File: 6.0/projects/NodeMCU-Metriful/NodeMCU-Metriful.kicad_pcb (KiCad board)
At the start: 2 copper layers, 5 parts, among them J3 DS18b20, J4 Particle, U1 NodeMCU_1.0_(ESP-12E), U2 Metriful-1

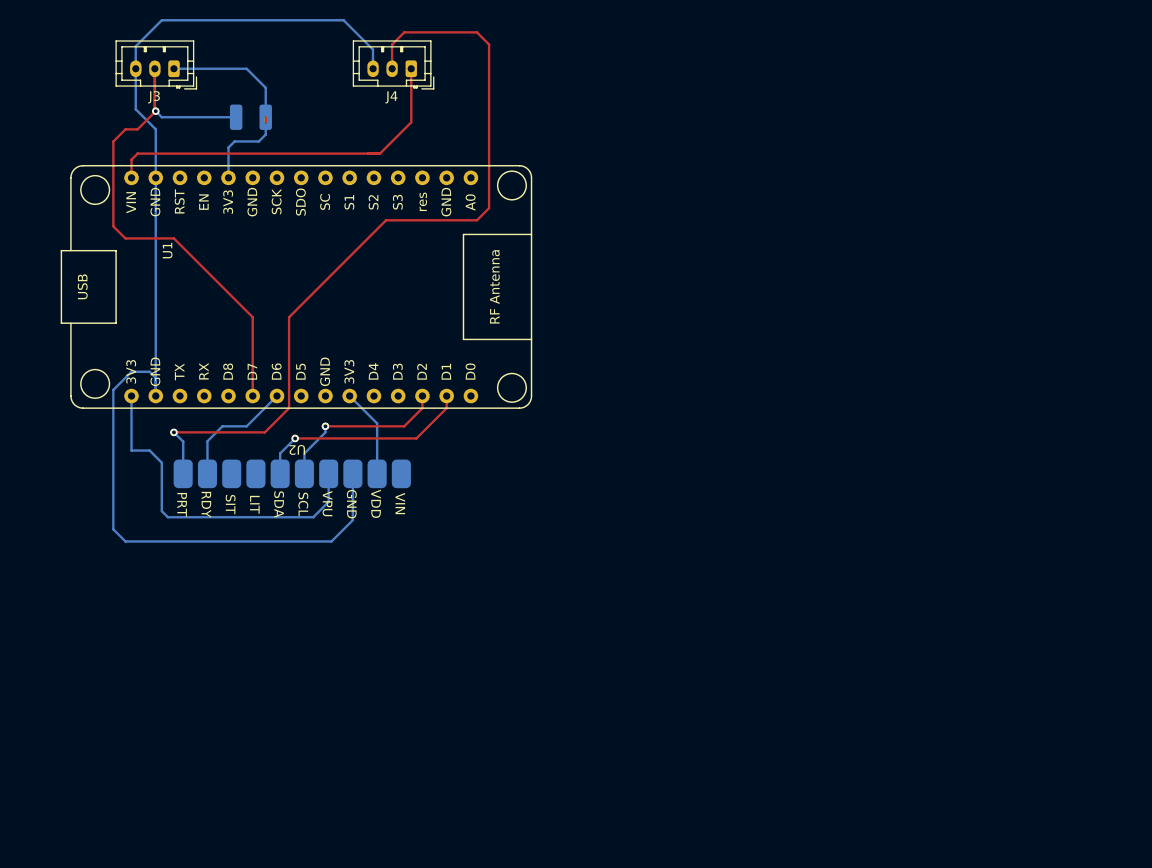
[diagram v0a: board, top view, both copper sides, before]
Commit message: Add NodeMCU-Metriful project
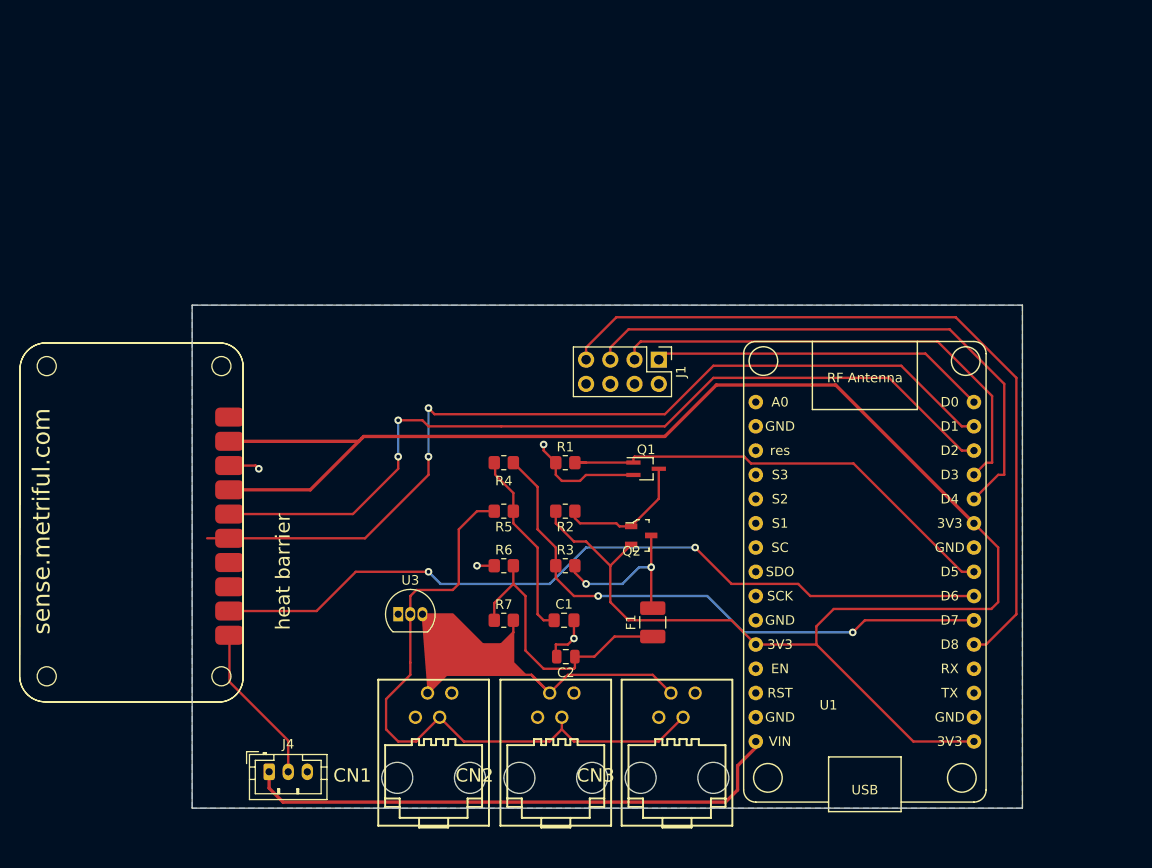
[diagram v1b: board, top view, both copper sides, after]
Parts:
- removed J3: DS18b20, Connector_JST:JST_PH_B3B-PH-K_1x03_P2.00mm_Vertical
- added C1: 100pF, Capacitor_SMD:C_0805_2012Metric_Pad1.18x1.45mm_HandSolder, F.Cu at (122.2, 95.9)
- added C2: 100nF, Capacitor_SMD:C_0805_2012Metric, F.Cu at (122.3, 99.7)
- added CN1: RJ10, 1wire-v0.4:rj10, F.Cu at (108.5, 111.5)
- added CN2: RJ10, 1wire-v0.4:rj10, F.Cu at (121.3, 111.5)
- added CN3: RJ10, 1wire-v0.4:rj10, F.Cu at (134.0, 111.5)
- added F1: Polyfuse_Small, Fuse:Fuse_1210_3225Metric_Pad1.42x2.65mm_HandSolder, F.Cu at (131.4, 96.1)
- added J1: Conn_02x04_Odd_Even, Connector_PinHeader_2.54mm:PinHeader_2x04_P2.54mm_Vertical, F.Cu at (132.1, 68.6)
- added Q1: BSS138BKW, Package_TO_SOT_SMD:SOT-323_SC-70_Handsoldering, F.Cu at (130.8, 80.0)
- added Q2: NX2301P, 1wire-v0.4:SOT-23-3, F.Cu at (130.2, 87.0)
- added R2: 10k, Resistor_SMD:R_0805_2012Metric_Pad1.20x1.40mm_HandSolder, F.Cu at (122.3, 84.5)
- added R3: 5.6k, Resistor_SMD:R_0805_2012Metric_Pad1.20x1.40mm_HandSolder, F.Cu at (122.3, 90.2)
- added R4: 22R, Resistor_SMD:R_0805_2012Metric_Pad1.20x1.40mm_HandSolder, F.Cu at (115.8, 79.4)
- added R5: 22R, Resistor_SMD:R_0805_2012Metric_Pad1.20x1.40mm_HandSolder, F.Cu at (115.8, 84.5)
- added R6: 10k, Resistor_SMD:R_0805_2012Metric_Pad1.20x1.40mm_HandSolder, F.Cu at (115.8, 90.2)
- added R7: 22R, Resistor_SMD:R_0805_2012Metric_Pad1.20x1.40mm_HandSolder, F.Cu at (115.8, 95.9)
- added U3: DS18B20, Package_TO_SOT_THT:TO-92_Inline, F.Cu at (104.8, 95.2)
- J4: value Particle -> Conn_01x03_Female
- R1: value 5.6k -> 10k; footprint Resistor_SMD:R_1210_3225Metric_Pad1.30x2.65mm_HandSolder -> Resistor_SMD:R_0805_2012Metric_Pad1.20x1.40mm_HandSolder; moved to F.Cu
- U2: moved to B.Cu
- moved J4 75.1 mm to (91.2, 111.8), turned to 0 degrees
- moved R1 48.9 mm to (122.3, 79.4), turned to 0 degrees
- moved U1 38.0 mm to (142.2, 73.0), turned to 0 degrees
- moved U2 28.4 mm to (88.4, 104.4), turned to -90 degrees
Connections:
- R1 pad 1: Net-(J3-Pad1) -> GND
- R1 pad 2: Net-(J3-Pad2) -> T_enable
- U1 pad 10: unconnected-(U1-Pad10) -> GND
- U1 pad 11: Net-(J3-Pad1) -> +3V3
- U1 pad 20: unconnected-(U1-Pad20) -> Net-(J1-Pad7)
- U1 pad 21: Net-(J3-Pad2) -> Net-(R3-Pad1)
- U1 pad 23: unconnected-(U1-Pad23) -> T_enable
- U1 pad 24: unconnected-(U1-Pad24) -> GND
- U1 pad 25: Net-(U1-Pad25) -> +3V3
- U1 pad 26: unconnected-(U1-Pad26) -> Net-(J1-Pad5)
- U1 pad 27: unconnected-(U1-Pad27) -> Net-(J1-Pad3)
- U1 pad 30: unconnected-(U1-Pad30) -> Net-(J1-Pad1)
- U2 pad 9: Net-(U1-Pad25) -> +3V3
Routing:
- net +3V3: track 35.8 -> 194.5 mm
- net GND: track 120.2 -> 23.0 mm, vias 0 -> 4
- net Net-(J1-Pad7): track 0.00 -> 80.8 mm
- net Net-(U1-Pad28): track 18.1 -> 91.1 mm, vias 1 -> 2
- net Net-(U1-Pad29): track 22.8 -> 95.1 mm, vias 1 -> 2
- net Net-(U1-Pad22): track 12.7 -> 83.9 mm, vias 0 -> 2
- net Net-(CN1-Pad3): track 0.00 -> 68.0 mm
- net Net-(J4-Pad2): track 84.0 -> 17.2 mm, vias 1 -> 0
- net Net-(R3-Pad1): track 0.00 -> 60.6 mm, vias 0 -> 2
- net Net-(J1-Pad5): track 0.00 -> 59.5 mm
- net Net-(J3-Pad2): track 59.0 -> 0.00 mm, vias 1 -> 0
- net Net-(J1-Pad3): track 0.00 -> 50.8 mm
- net T_enable: track 0.00 -> 48.5 mm
- net Net-(CN1-Pad2): track 0.00 -> 47.5 mm
- net Net-(J1-Pad1): track 0.00 -> 35.4 mm
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- added copper zone on B.Cu, net GND
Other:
- board outline added: 87 x 52.7 mm
- board text added: "heat barrier"

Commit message: Made print smaller, moved RJ10 upwards, as they're straight Also discovered that my NodeMCUs are WIDER. So this is before that change.
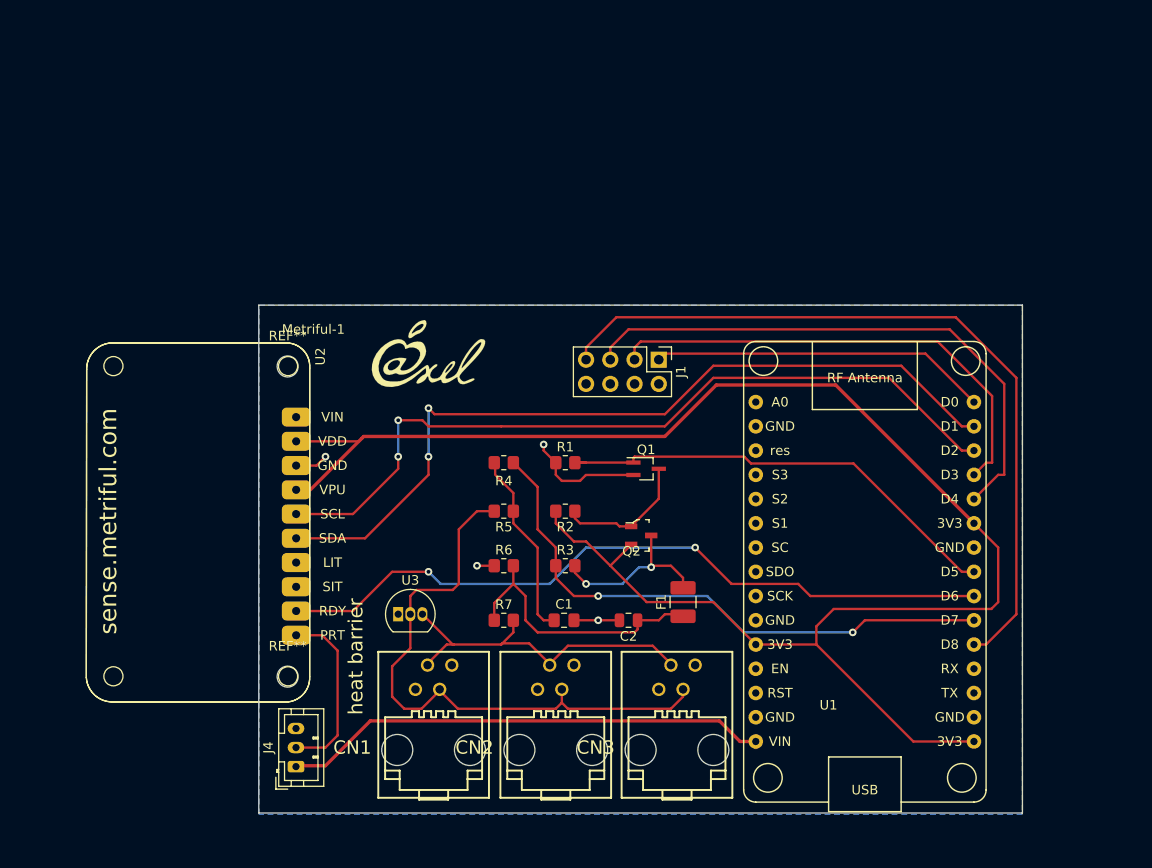
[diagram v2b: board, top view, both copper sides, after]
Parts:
- added G***: LOGO, ESP-RS232:LOGO2, F.Cu at (108.0, 67.9)
- added REF**: MountingHole_2.2mm_M2, MountingHole:MountingHole_2.2mm_M2, F.Cu at (93.2, 69.3)
- added REF**: MountingHole_2.2mm_M2, MountingHole:MountingHole_2.2mm_M2, F.Cu at (93.2, 101.8)
- U2: footprint Sensor:Metriful_SMD-1 -> Sensor:Metriful-1; moved to F.Cu
- moved C2 7.59 mm to (128.9, 95.9)
- moved U2 6.98 mm to (95.4, 104.4), turned to 90 degrees
- moved F1 3.82 mm to (134.6, 94.0)
- moved CN1 2.92 mm to (108.5, 108.6)
- moved CN3 2.92 mm to (134.0, 108.6)
- moved CN2 2.92 mm to (121.3, 108.6)
- moved J4 2.87 mm to (94.1, 111.2), turned to 90 degrees
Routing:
- net +3V3: track 194.5 -> 177.5 mm
- net Net-(CN1-Pad2): track 47.5 -> 36.9 mm
- net Net-(U1-Pad29): track 95.1 -> 85.8 mm
- net Net-(U1-Pad22): track 83.9 -> 76.9 mm
- net Net-(U1-Pad28): track 91.1 -> 84.1 mm
- net VDD: track 57.8 -> 51.7 mm
- net Net-(CN1-Pad3): track 68.0 -> 62.7 mm
- net Net-(J4-Pad2): track 17.2 -> 19.1 mm
- net Net-(C2-Pad1): track 30.5 -> 29.6 mm
- net Net-(F1-Pad2): track 17.6 -> 18.3 mm
- net GND: track 23.0 -> 22.4 mm
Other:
- board size 87 x 52.7 mm -> 80 x 53.2 mm

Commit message: Final (?) version, eliminated the severe warnings.
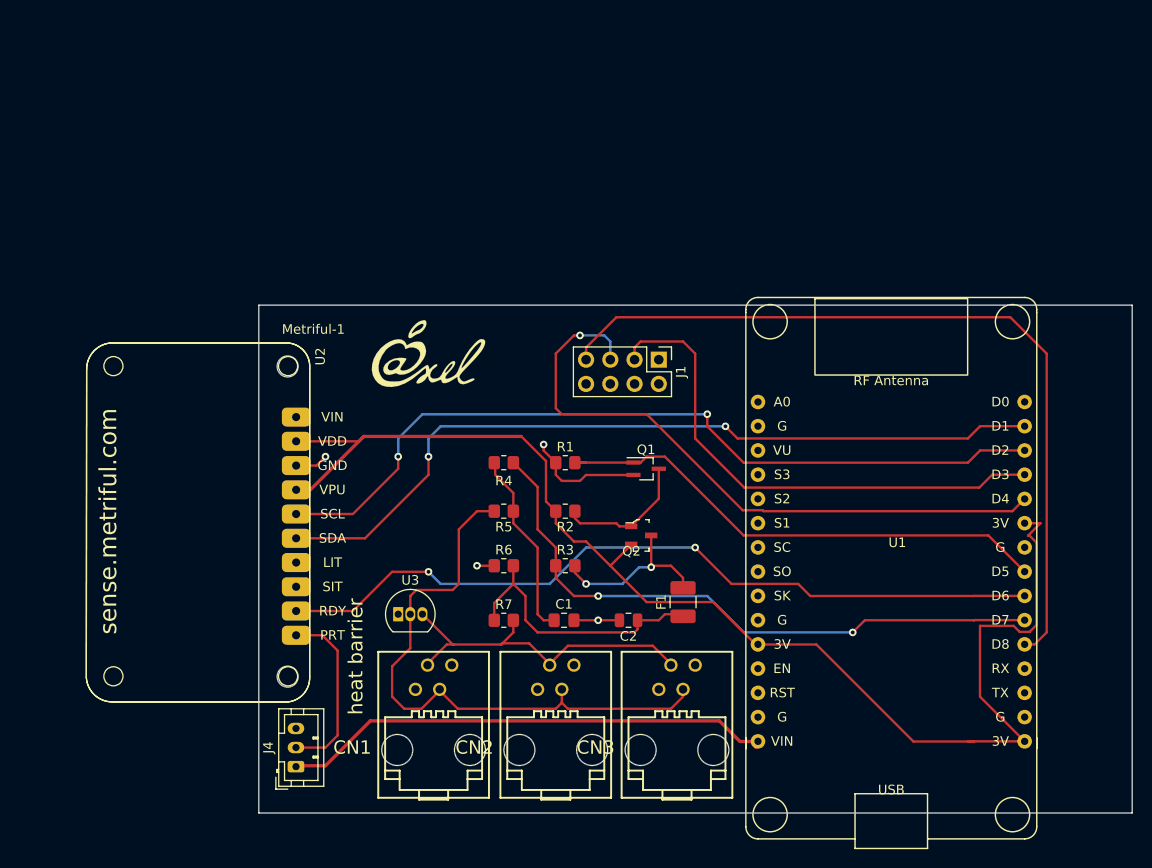
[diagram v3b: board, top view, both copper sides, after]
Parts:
- U1: footprint Module:NodeMCU1.0(12-E) -> NodeMCU:NodeMCU_0.1_Axel
- moved U1 22.7 mm to (156.4, 90.8)
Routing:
- net +3V3: track 177.5 -> 139.7 mm
- net Net-(J1-Pad1): track 35.4 -> 0.90 mm
- net Net-(J1-Pad5): track 59.5 -> 68.7 mm, vias 0 -> 1
- net Net-(U1-Pad22): track 76.9 -> 82.2 mm
- net Net-(R3-Pad1): track 60.6 -> 65.9 mm
- net T_enable: track 48.5 -> 53.6 mm
- net Net-(J1-Pad7): track 80.8 -> 84.7 mm
- net Net-(J1-Pad3): track 50.8 -> 54.5 mm
- net Net-(U1-Pad28): track 84.1 -> 86.5 mm
- net Net-(U1-Pad29): track 85.8 -> 84.5 mm
- removed copper zone on B.Cu, net GND
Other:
- board size 80 x 53.2 mm -> 91.5 x 53.2 mm
